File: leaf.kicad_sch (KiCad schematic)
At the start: 0 parts

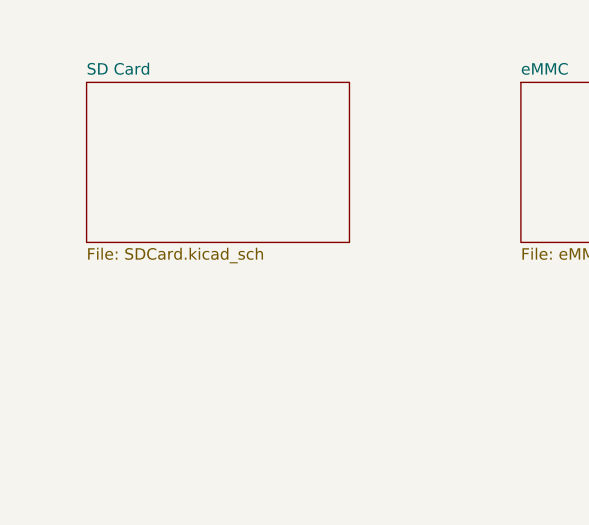
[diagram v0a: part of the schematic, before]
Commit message: added MicroSD
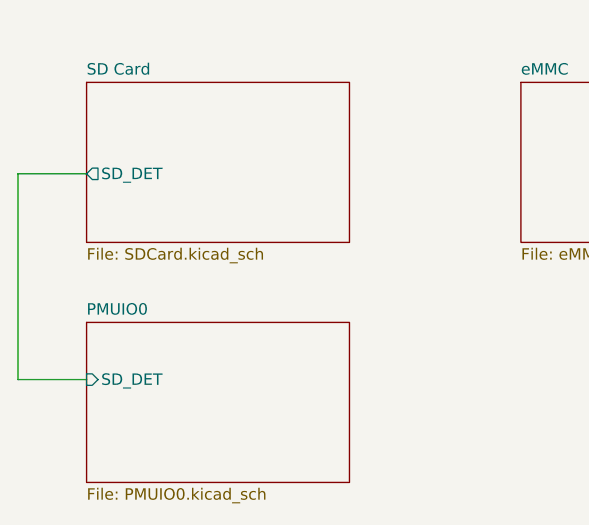
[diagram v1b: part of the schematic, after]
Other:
- added sheet PMUIO0 (PMUIO0.kicad_sch)
- sheet SD Card ports: added SD_DET; removed none
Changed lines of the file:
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@@
     (company "Qingdao IotPi Information Technology")
+  )
+  (wire (pts (xy 33.02 80.01) (xy 25.4 80.01))
+    (stroke (width 0) (type default))
+  )
+  (wire (pts (xy 25.4 102.87) (xy 33.02 102.87))
+    (stroke (width 0) (type default))
+  )
+  (wire (pts (xy 25.4 80.01) (xy 25.4 102.87))
+    (stroke (width 0) (type default))
   )
   (sheet (at 81.28 69.85) (size 29.21 17.78) (fields_autoplaced)
@@
     )
   )
+  (sheet (at 33.02 96.52) (size 29.21 17.78) (fields_autoplaced)
+    (stroke (width 0.1524) (type solid))
+    (fill (color 0 0 0 0.0000))
+    (property "Sheetname" "PMUIO0" (at 33.02 95.8084 0)
+      (effects (font (size 1.27 1.27)) (justify left bottom))
+    )
+    (property "Sheetfile" "PMUIO0.kicad_sch" (at 33.02 114.8846 0)
+      (effects (font (size 1.27 1.27)) (justify left top))
+    )
+    (pin "SD_DET" input (at 33.02 102.87 180)
+      (effects (font (size 1.27 1.27)) (justify left))
+    )
+    (instances
+      (project "leaf"
+        (path "/e3b58043-16a3-43c8-9fad-9c9784eebfa4" (page "20"))
+      )
+    )
+  )
   (sheet (at 33.02 69.85) (size 29.21 17.78) (fields_autoplaced)
     (stroke (width 0.1524) (type solid))
@@
       (effects (font (size 1.27 1.27)) (justify left top))
     )
+    (pin "SD_DET" output (at 33.02 80.01 180)
+      (effects (font (size 1.27 1.27)) (justify left))
+    )
     (instances

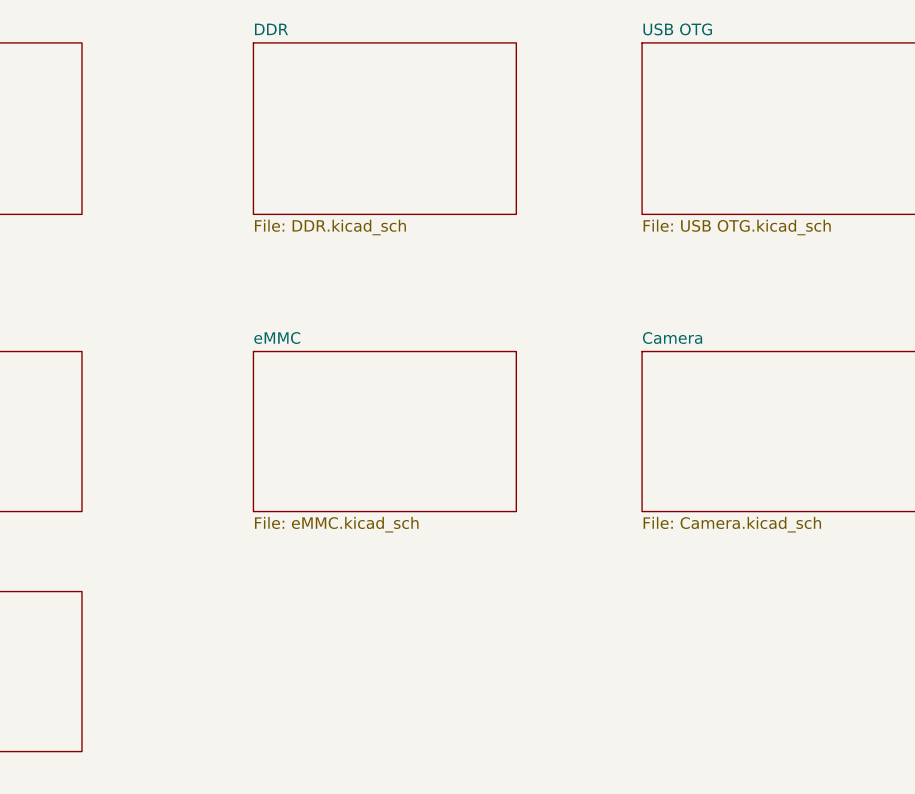
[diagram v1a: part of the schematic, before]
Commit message: updated USB
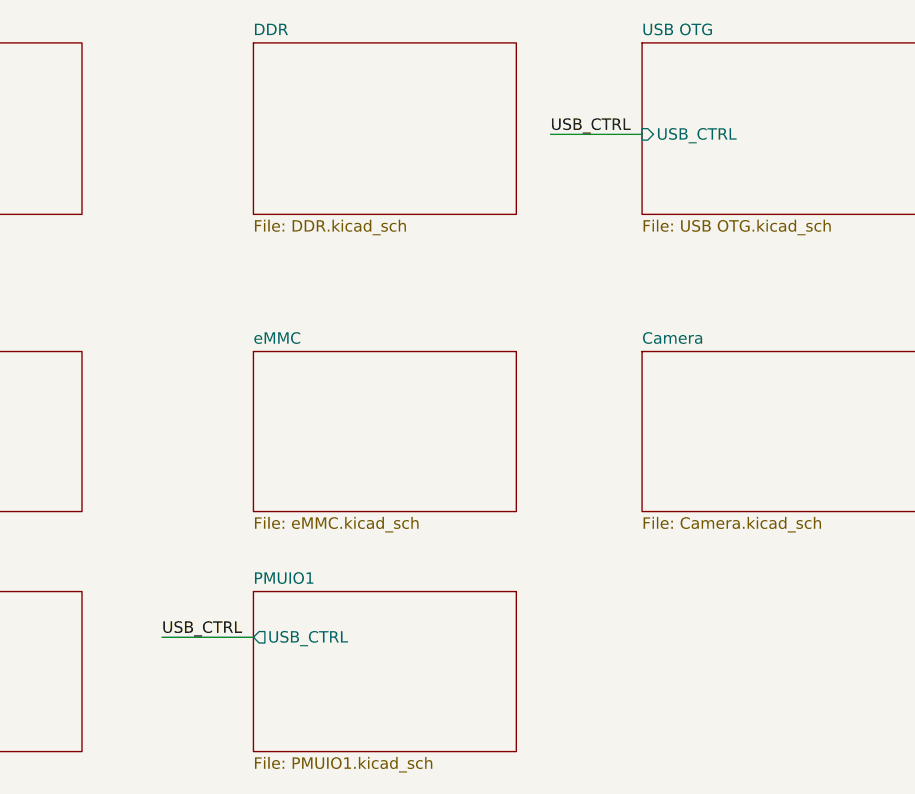
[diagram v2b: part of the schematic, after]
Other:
- added sheet PMUIO1 (PMUIO1.kicad_sch)
- sheet USB OTG ports: added USB_CTRL; removed none
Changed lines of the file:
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@@
     (company "Qingdao IotPi Information Technology")
   )
+  (wire (pts (xy 71.12 101.6) (xy 81.28 101.6))
+    (stroke (width 0) (type default))
+  )
   (wire (pts (xy 33.02 80.01) (xy 25.4 80.01))
+    (stroke (width 0) (type default))
+  )
+  (wire (pts (xy 114.3 45.72) (xy 124.46 45.72))
     (stroke (width 0) (type default))
   )
@@
   (wire (pts (xy 25.4 80.01) (xy 25.4 102.87))
     (stroke (width 0) (type default))
+  )
+  (label "USB_CTRL" (at 71.12 101.6 0) (fields_autoplaced)
+    (effects (font (size 1.27 1.27)) (justify left bottom))
+  )
+  (label "USB_CTRL" (at 114.3 45.72 0) (fields_autoplaced)
+    (effects (font (size 1.27 1.27)) (justify left bottom))
   )
   (sheet (at 81.28 69.85) (size 29.21 17.78) (fields_autoplaced)
@@
       (project "leaf"
         (path "/e3b58043-16a3-43c8-9fad-9c9784eebfa4" (page "5"))
+      )
+    )
+  )
+  (sheet (at 81.28 96.52) (size 29.21 17.78) (fields_autoplaced)
+    (stroke (width 0.1524) (type solid))
+    (fill (color 0 0 0 0.0000))
+    (property "Sheetname" "PMUIO1" (at 81.28 95.8084 0)
+      (effects (font (size 1.27 1.27)) (justify left bottom))
+    )
+    (property "Sheetfile" "PMUIO1.kicad_sch" (at 81.28 114.8846 0)
+      (effects (font (size 1.27 1.27)) (justify left top))
+    )
+    (pin "USB_CTRL" output (at 81.28 101.6 180)
+      (effects (font (size 1.27 1.27)) (justify left))
+    )
+    (instances
+      (project "leaf"
+        (path "/e3b58043-16a3-43c8-9fad-9c9784eebfa4" (page "21"))
       )
     )
@@
       (effects (font (size 1.27 1.27)) (justify left top))
     )
+    (pin "USB_CTRL" input (at 124.46 45.72 180)
+      (effects (font (size 1.27 1.27)) (justify left))
+    )
     (instances

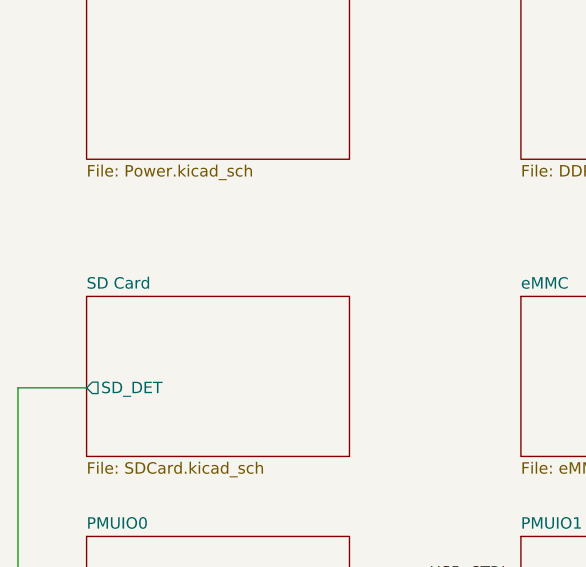
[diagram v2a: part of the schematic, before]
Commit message: Rename SDCard sheet
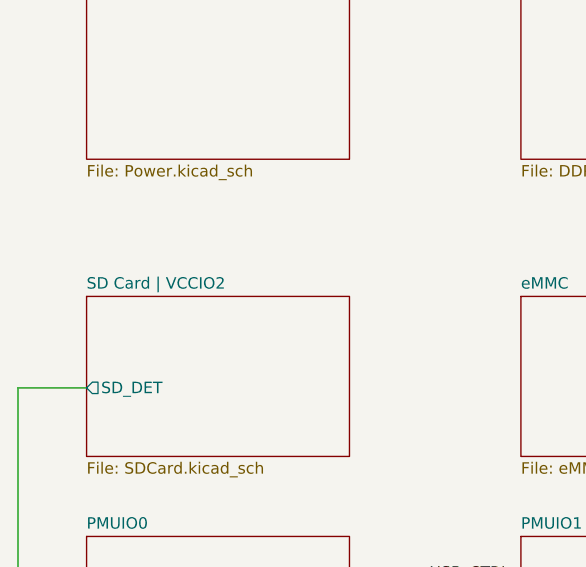
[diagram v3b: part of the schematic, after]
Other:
- sheet SD Card renamed SD Card | VCCIO2
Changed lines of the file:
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@@
     (stroke (width 0.1524) (type solid))
     (fill (color 0 0 0 0.0000))
-    (property "Sheetname" "SD Card" (at 33.02 69.1384 0)
+    (property "Sheetname" "SD Card | VCCIO2" (at 33.02 69.1384 0)
       (effects (font (size 1.27 1.27)) (justify left bottom))
     )

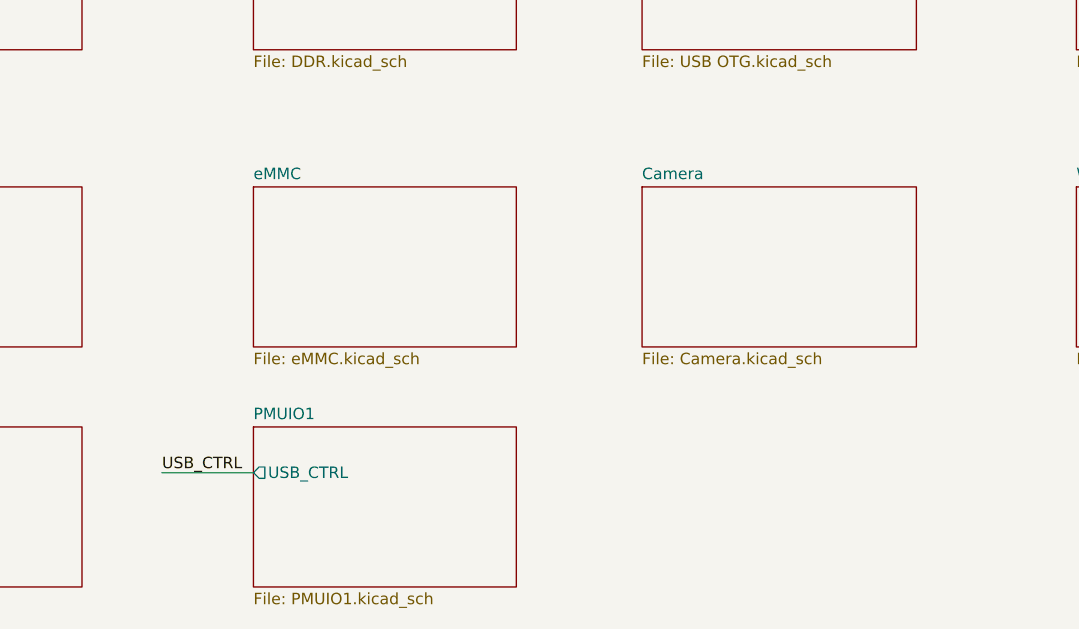
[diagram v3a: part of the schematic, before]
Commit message: added blank Ethernet
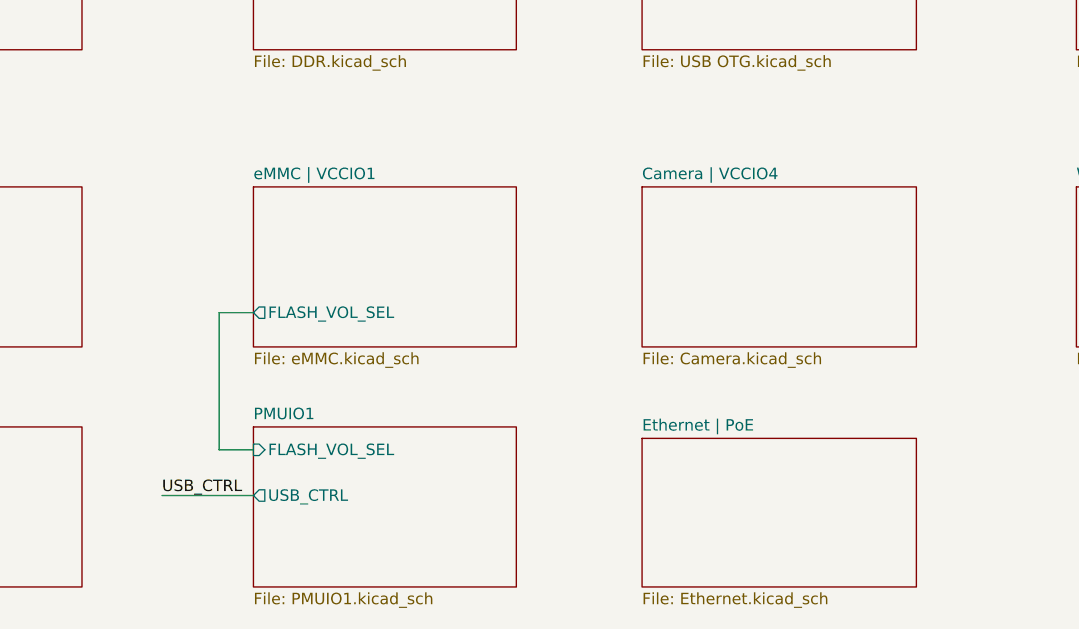
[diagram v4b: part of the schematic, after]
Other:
- sheet Camera renamed Camera | VCCIO4
- sheet eMMC renamed eMMC | VCCIO1
- added sheet Ethernet | PoE (Ethernet.kicad_sch)
- sheet PMUIO1 ports: added FLASH_VOL_SEL; removed none
- sheet eMMC | VCCIO1 ports: added FLASH_VOL_SEL; removed none
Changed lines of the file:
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@@
     (company "Qingdao IotPi Information Technology")
   )
-  (wire (pts (xy 71.12 101.6) (xy 81.28 101.6))
+  (wire (pts (xy 71.12 104.14) (xy 81.28 104.14))
+    (stroke (width 0) (type default))
+  )
+  (wire (pts (xy 77.47 99.06) (xy 77.47 83.82))
+    (stroke (width 0) (type default))
+  )
+  (wire (pts (xy 81.28 99.06) (xy 77.47 99.06))
+    (stroke (width 0) (type default))
+  )
+  (wire (pts (xy 77.47 83.82) (xy 81.28 83.82))
     (stroke (width 0) (type default))
   )
@@
     (stroke (width 0) (type default))
   )
-  (label "USB_CTRL" (at 71.12 101.6 0) (fields_autoplaced)
+  (label "USB_CTRL" (at 71.12 104.14 0) (fields_autoplaced)
     (effects (font (size 1.27 1.27)) (justify left bottom))
   )
@@
     (stroke (width 0.1524) (type solid))
     (fill (color 0 0 0 0.0000))
-    (property "Sheetname" "eMMC" (at 81.28 69.1384 0)
+    (property "Sheetname" "eMMC | VCCIO1" (at 81.28 69.1384 0)
       (effects (font (size 1.27 1.27)) (justify left bottom))
     )
     (property "Sheetfile" "eMMC.kicad_sch" (at 81.28 88.2146 0)
       (effects (font (size 1.27 1.27)) (justify left top))
+    )
+    (pin "FLASH_VOL_SEL" output (at 81.28 83.82 180)
+      (effects (font (size 1.27 1.27)) (justify left))
     )
     (instances
@@
       (effects (font (size 1.27 1.27)) (justify left top))
     )
-    (pin "USB_CTRL" output (at 81.28 101.6 180)
+    (pin "USB_CTRL" output (at 81.28 104.14 180)
+      (effects (font (size 1.27 1.27)) (justify left))
+    )
+    (pin "FLASH_VOL_SEL" input (at 81.28 99.06 180)
       (effects (font (size 1.27 1.27)) (justify left))
     )
@@
     )
   )
+  (sheet (at 124.46 97.79) (size 30.48 16.51) (fields_autoplaced)
+    (stroke (width 0.1524) (type solid))
+    (fill (color 0 0 0 0.0000))
+    (property "Sheetname" "Ethernet | PoE" (at 124.46 97.0784 0)
+      (effects (font (size 1.27 1.27)) (justify left bottom))
+    )
+    (property "Sheetfile" "Ethernet.kicad_sch" (at 124.46 114.8846 0)
+      (effects (font (size 1.27 1.27)) (justify left top))
+    )
+    (instances
+      (project "leaf"
+        (path "/e3b58043-16a3-43c8-9fad-9c9784eebfa4" (page "22"))
+      )
+    )
+  )
   (sheet (at 124.46 69.85) (size 30.48 17.78) (fields_autoplaced)
     (stroke (width 0.1524) (type solid))
     (fill (color 0 0 0 0.0000))
-    (property "Sheetname" "Camera" (at 124.46 69.1384 0)
+    (property "Sheetname" "Camera | VCCIO4" (at 124.46 69.1384 0)
       (effects (font (size 1.27 1.27)) (justify left bottom))
     )

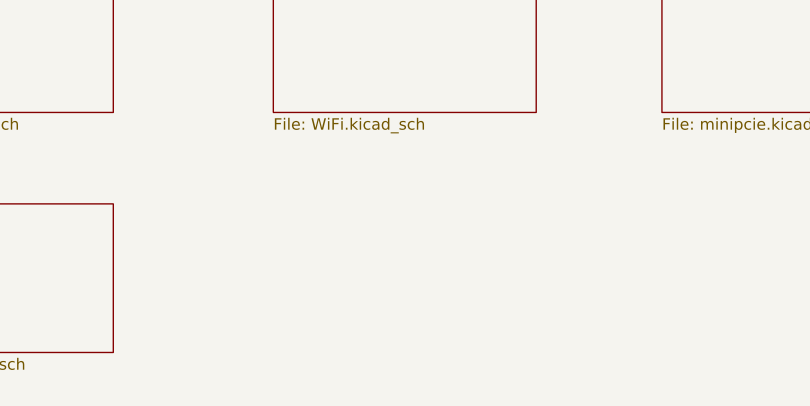
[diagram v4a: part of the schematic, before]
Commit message: added missing pins
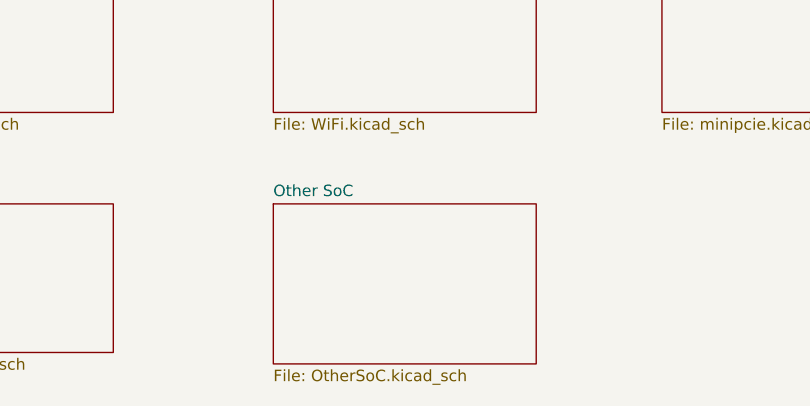
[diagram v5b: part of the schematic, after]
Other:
- added sheet Other SoC (OtherSoC.kicad_sch)
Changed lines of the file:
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@@
+    )
+  )
+  (sheet (at 172.72 97.79) (size 29.21 17.78) (fields_autoplaced)
+    (stroke (width 0.1524) (type solid))
+    (fill (color 0 0 0 0.0000))
+    (property "Sheetname" "Other SoC" (at 172.72 97.0784 0)
+      (effects (font (size 1.27 1.27)) (justify left bottom))
+    )
+    (property "Sheetfile" "OtherSoC.kicad_sch" (at 172.72 116.1546 0)
+      (effects (font (size 1.27 1.27)) (justify left top))
+    )
+    (instances
+      (project "leaf"
+        (path "/e3b58043-16a3-43c8-9fad-9c9784eebfa4" (page "23"))
+      )
     )
   )
